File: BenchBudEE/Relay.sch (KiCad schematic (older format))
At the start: 0 parts

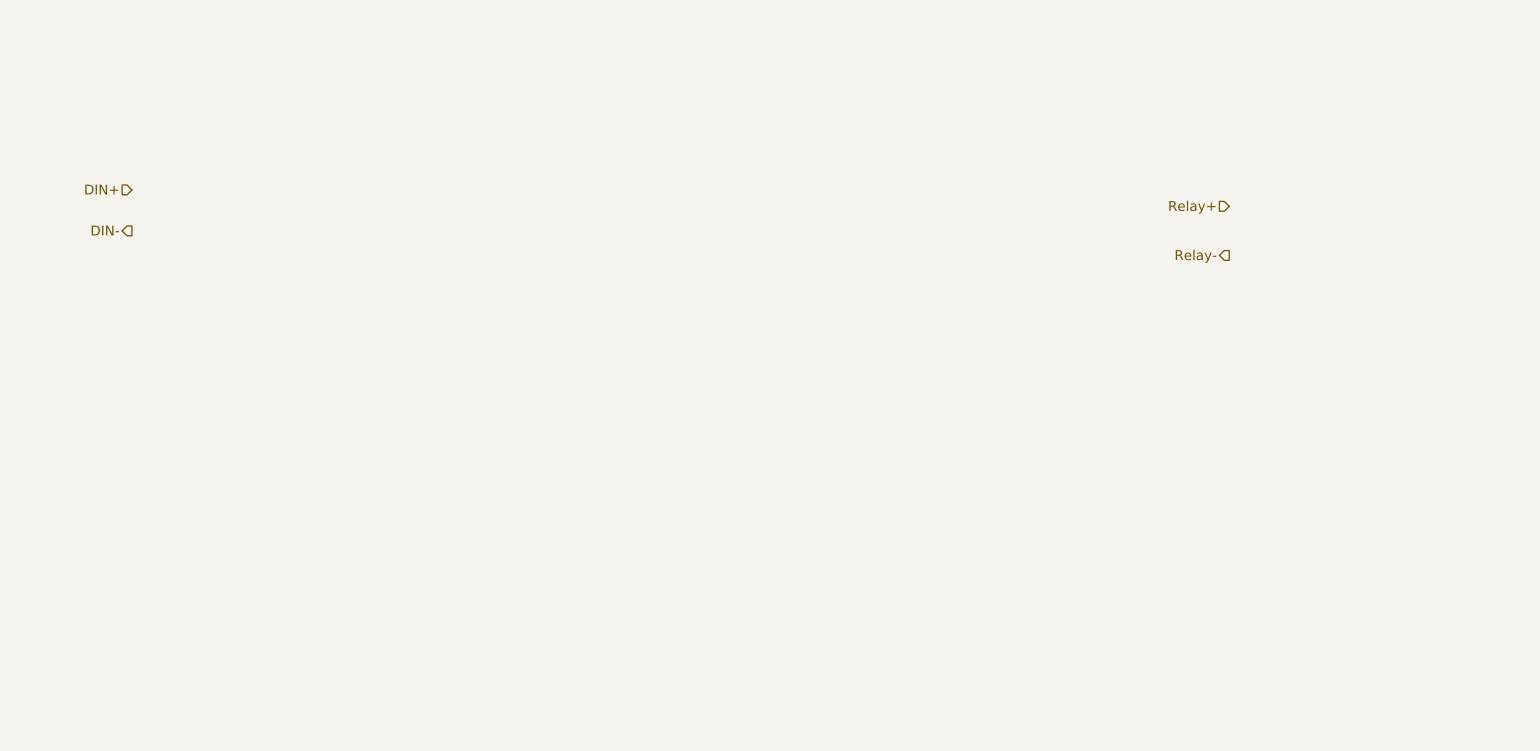
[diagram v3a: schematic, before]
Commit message: Roughly filled in the Relay sheet.
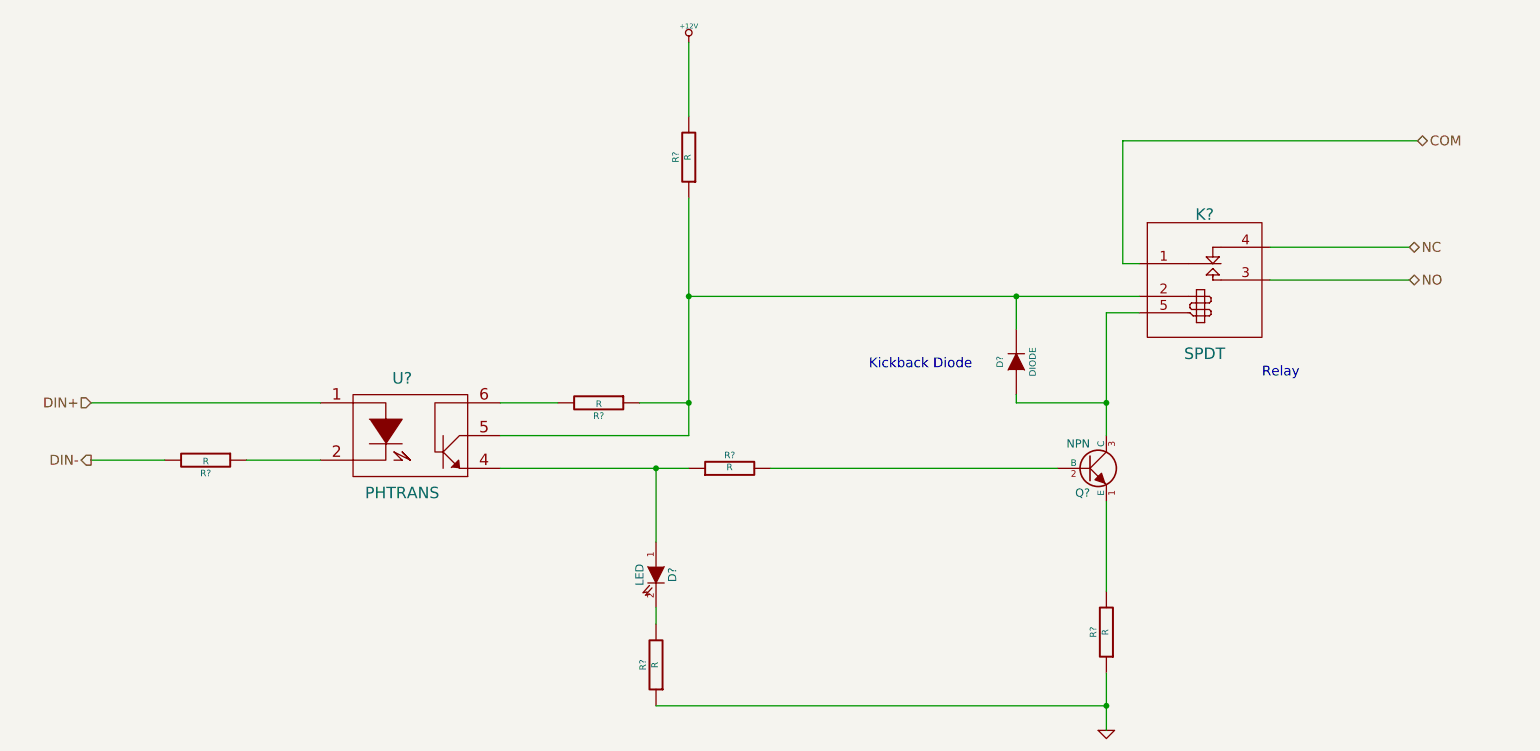
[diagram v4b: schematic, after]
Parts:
- added D?: LED, ~, symbol LED
- added D?: DIODE, ~, symbol DIODE
- added K?: SPDT, ~, symbol SPDT
- added Q?: NPN, ~, symbol NPN
- added R? (x6): R, ~, symbol R
- added U?: PHTRANS, ~, symbol PHTRANS
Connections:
- net DIN+: now also U?.1
- net DIN-: now also R?.2
- new net: R?.1, U?.2
- new net: D?.1 (A), R?.1, U?.4
- new net: D?.2 (K), K?.2 (COIL+), R?.1, R?.1, U?.5
- new net: R?.2, U?.6
- new net: Q?.2 (B), R?.2
- new net: Q?.1 (E), R?.2
- new net: D?.1 (A), K?.5 (COIL-), Q?.3 (C)
- new net: D?.2 (K), R?.2
- new net +12V: R?.2
- new net COM: K?.1 (COM)
- new net GND: R?.1, R?.1
- new net NC: K?.4 (NC)
- new net NO: K?.3 (NO)
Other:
- note added: "Kickback Diode"
- note added: "Relay"
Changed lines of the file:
@@
 LIBS:contrib
 LIBS:valves
+LIBS:BenchBudEE
 LIBS:BenchBudEE-cache
 EELAYER 27 0
@@
 Sheet 4 8
 Title ""
-Date "6 feb 2014"
+Date "7 feb 2014"
 Rev ""
 Comp ""
@@
 Comment4 ""
 $EndDescr
-Text HLabel 2100 2850 0    60   Input ~ 0
+Text HLabel 1850 4150 0    60   Input ~ 0
 DIN+
-Text HLabel 2100 3100 0    60   Output ~ 0
+Text HLabel 1850 4500 0    60   Output ~ 0
 DIN-
-Text HLabel 8800 2950 0    60   Input ~ 0
-Relay+
-Text HLabel 8800 3250 0    60   Output ~ 0
-Relay-
+Text HLabel 9900 3200 2    60   BiDi ~ 0
+NC
+Text HLabel 9900 3400 2    60   BiDi ~ 0
+NO
+$Comp
+L PHTRANS U?
+U 1 1 52F440BD
+P 3800 4350
+F 0 "U?" H 3750 4700 70  0000 C CNN
+F 1 "PHTRANS" H 3750 4000 70  0000 C CNN
+F 2 "~" H 3800 4350 60  0000 C CNN
+F 3 "~" H 3800 4350 60  0000 C CNN
+	1    3800 4350
+	1    0    0    -1
+$EndComp
+$Comp
+L R R?
+U 1 1 52F440DB
+P 5750 4550
+F 0 "R?" V 5830 4550 40  0000 C CNN
+F 1 "R" V 5757 4551 40  0000 C CNN
+F 2 "~" V 5680 4550 30  0000 C CNN
+F 3 "~" H 5750 4550 30  0000 C CNN
+	1    5750 4550
+	0    -1   -1   0
+$EndComp
+$Comp
+L NPN Q?
+U 1 1 52F440EA
+P 7950 4550
+F 0 "Q?" H 7950 4400 50  0000 R CNN
+F 1 "NPN" H 7950 4700 50  0000 R CNN
+F 2 "~" H 7950 4550 60  0000 C CNN
+F 3 "~" H 7950 4550 60  0000 C CNN
+	1    7950 4550
+	1    0    0    -1
+$EndComp
+$Comp
+L LED D?
+U 1 1 52F440F9
+P 5300 5200
+F 0 "D?" H 5300 5300 50  0000 C CNN
+F 1 "LED" H 5300 5100 50  0000 C CNN
+F 2 "~" H 5300 5200 60  0000 C CNN
+F 3 "~" H 5300 5200 60  0000 C CNN
+	1    5300 5200
+	0    1    1    0
+$EndComp
+$Comp
+L SPDT K?
+U 1 1 52F44639
+P 8650 3250
+F 0 "K?" H 8650 3500 70  0000 C CNN
+F 1 "SPDT" H 8650 2650 70  0000 C CNN
+F 2 "~" H 8650 3250 60  0000 C CNN
+F 3 "~" H 8650 3250 60  0000 C CNN
+	1    8650 3250
+	1    0    0    -1
+$EndComp
+Text HLabel 9950 2550 2    60   BiDi ~ 0
+COM
+Wire Wire Line
+	9050 3200 9900 3200
+Wire Wire Line
+	9050 3400 9900 3400
+Wire Wire Line
+	4350 4550 5500 4550
+Wire Wire Line
+	6000 4550 7750 4550
+Wire Wire Line
+	5500 3500 8250 3500
+Wire Wire Line
+	8050 4750 8050 5300
+$Comp
+L R R?
+U 1 1 52F448EE
+P 8050 5550
+F 0 "R?" V 8130 5550 40  0000 C CNN
+F 1 "R" V 8057 5551 40  0000 C CNN
+F 2 "~" V 7980 5550 30  0000 C CNN
+F 3 "~" H 8050 5550 30  0000 C CNN
+	1    8050 5550
+	-1   0    0    1
+$EndComp
+$Comp
+L GND #PWR?
+U 1 1 52F448F6
+P 8050 6150
+F 0 "#PWR?" H 8050 6150 30  0001 C CNN
+F 1 "GND" H 8050 6080 30  0001 C CNN
+F 2 "" H 8050 6150 60  0000 C CNN
+F 3 "" H 8050 6150 60  0000 C CNN
+	1    8050 6150
+	1    0    0    -1
+$EndComp
+Wire Wire Line
+	8050 5800 8050 6150
+Wire Wire Line
+	5500 2900 5500 4350
+Wire Wire Line
+	5300 5000 5300 4550
+Connection ~ 5300 4550
+$Comp
+L R R?
+U 1 1 52F44A66
+P 5300 5750
+F 0 "R?" V 5380 5750 40  0000 C CNN
+F 1 "R" V 5307 5751 40  0000 C CNN
+F 2 "~" V 5230 5750 30  0000 C CNN
+F 3 "~" H 5300 5750 30  0000 C CNN
+	1    5300 5750
+	-1   0    0    1
+$EndComp
+Wire Wire Line
+	5300 5500 5300 5400
+Wire Wire Line
+	5300 6000 8050 6000
+Connection ~ 8050 6000
+$Comp
+L R R?
+U 1 1 52F44A89
+P 5500 2650
+F 0 "R?" V 5580 2650 40  0000 C CNN
+F 1 "R" V 5507 2651 40  0000 C CNN
+F 2 "~" V 5430 2650 30  0000 C CNN
+F 3 "~" H 5500 2650 30  0000 C CNN
+	1    5500 2650
+	-1   0    0    1
+$EndComp
+$Comp
+L +12V #PWR?
+U 1 1 52F44A91
+P 5500 1950
+F 0 "#PWR?" H 5500 1900 20  0001 C CNN
+F 1 "+12V" H 5500 2050 30  0000 C CNN
+F 2 "" H 5500 1950 60  0000 C CNN
+F 3 "" H 5500 1950 60  0000 C CNN
+	1    5500 1950
+	1    0    0    -1
+$EndComp
+Wire Wire Line
+	5500 1950 5500 2400
+Wire Wire Line
+	5500 4350 4350 4350
+Connection ~ 5500 3500
+$Comp
+L R R?
+U 1 1 52F44ACB
+P 4950 4150
+F 0 "R?" V 5030 4150 40  0000 C CNN
+F 1 "R" V 4957 4151 40  0000 C CNN
+F 2 "~" V 4880 4150 30  0000 C CNN
+F 3 "~" H 4950 4150 30  0000 C CNN
+	1    4950 4150
+	0    1    1    0
+$EndComp
+Wire Wire Line
+	4350 4150 4700 4150
+Wire Wire Line
+	5200 4150 5500 4150
+Connection ~ 5500 4150
+$Comp
+L R R?
+U 1 1 52F44AFE
+P 2550 4500
+F 0 "R?" V 2630 4500 40  0000 C CNN
+F 1 "R" V 2557 4501 40  0000 C CNN
+F 2 "~" V 2480 4500 30  0000 C CNN
+F 3 "~" H 2550 4500 30  0000 C CNN
+	1    2550 4500
+	0    1    1    0
+$EndComp
+Wire Wire Line
+	2800 4500 3250 4500
+Wire Wire Line
+	1850 4500 2300 4500
+Wire Wire Line
+	1850 4150 3250 4150
+Wire Wire Line
+	9950 2550 8150 2550
+Wire Wire Line
+	8150 2550 8150 3300
+Wire Wire Line
+	8150 3300 8250 3300
+Wire Wire Line
+	8050 4350 8050 3600
+Wire Wire Line
+	8050 3600 8250 3600
+$Comp
+L DIODE D?
+U 1 1 52F44F61
+P 7500 3900
+F 0 "D?" H 7500 4000 40  0000 C CNN
+F 1 "DIODE" H 7500 3800 40  0000 C CNN
+F 2 "~" H 7500 3900 60  0000 C CNN
+F 3 "~" H 7500 3900 60  0000 C CNN
+	1    7500 3900
+	0    -1   -1   0
+$EndComp
+Wire Wire Line
+	7500 3700 7500 3500
+Connection ~ 7500 3500
+Wire Wire Line
+	7500 4100 7500 4150
+Wire Wire Line
+	7500 4150 8050 4150
+Connection ~ 8050 4150
+Text Notes 6600 3950 0    60   ~ 0
+Kickback Diode
+Text Notes 9000 4000 0    60   ~ 0
+Relay
 $EndSCHEMATC

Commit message: Roughly populated the Power sheet.
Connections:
- net +12V renamed +12P
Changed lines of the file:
@@
 $Descr A4 11693 8268
 encoding utf-8
-Sheet 4 8
+Sheet 4 9
 Title ""
-Date "7 feb 2014"
+Date "8 feb 2014"
 Rev ""
 Comp ""
@@
 	-1   0    0    1
 $EndComp
-$Comp
-L +12V #PWR?
-U 1 1 52F44A91
-P 5500 1950
-F 0 "#PWR?" H 5500 1900 20  0001 C CNN
-F 1 "+12V" H 5500 2050 30  0000 C CNN
-F 2 "" H 5500 1950 60  0000 C CNN
-F 3 "" H 5500 1950 60  0000 C CNN
-	1    5500 1950
-	1    0    0    -1
-$EndComp
-Wire Wire Line
-	5500 1950 5500 2400
+Wire Wire Line
+	5500 1900 5500 2400
 Wire Wire Line
 	5500 4350 4350 4350
@@
 Text Notes 9000 4000 0    60   ~ 0
 Relay
+$Comp
+L +12P #PWR?
+U 1 1 52F62CEB
+P 5500 1900
+F 0 "#PWR?" H 5500 1870 30  0001 C CNN
+F 1 "+12P" H 5500 2000 30  0000 C CNN
+F 2 "" H 5500 1900 60  0000 C CNN
+F 3 "" H 5500 1900 60  0000 C CNN
+	1    5500 1900
+	1    0    0    -1
+$EndComp
 $EndSCHEMATC

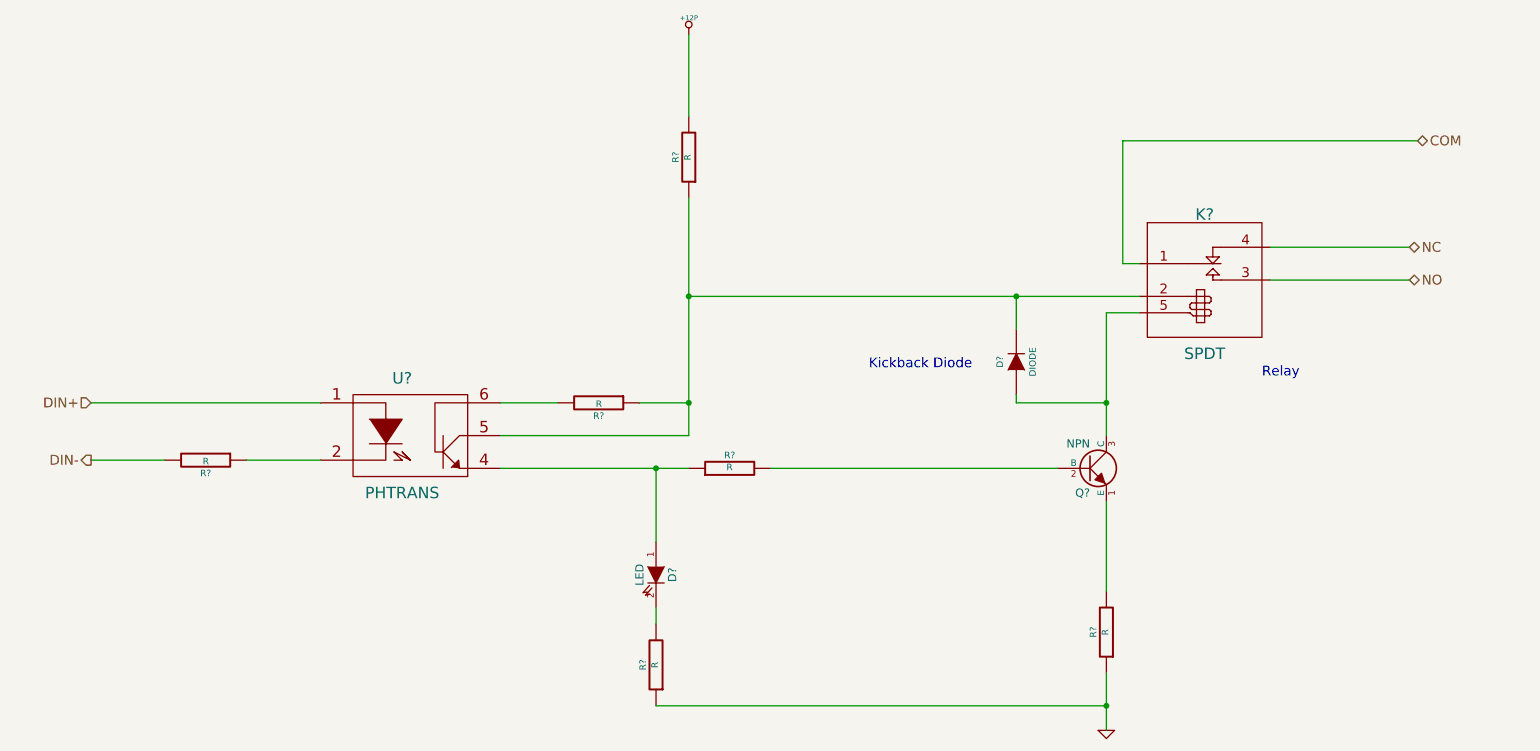
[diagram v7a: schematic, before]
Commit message: Populated the Arduino block and top level wiring.
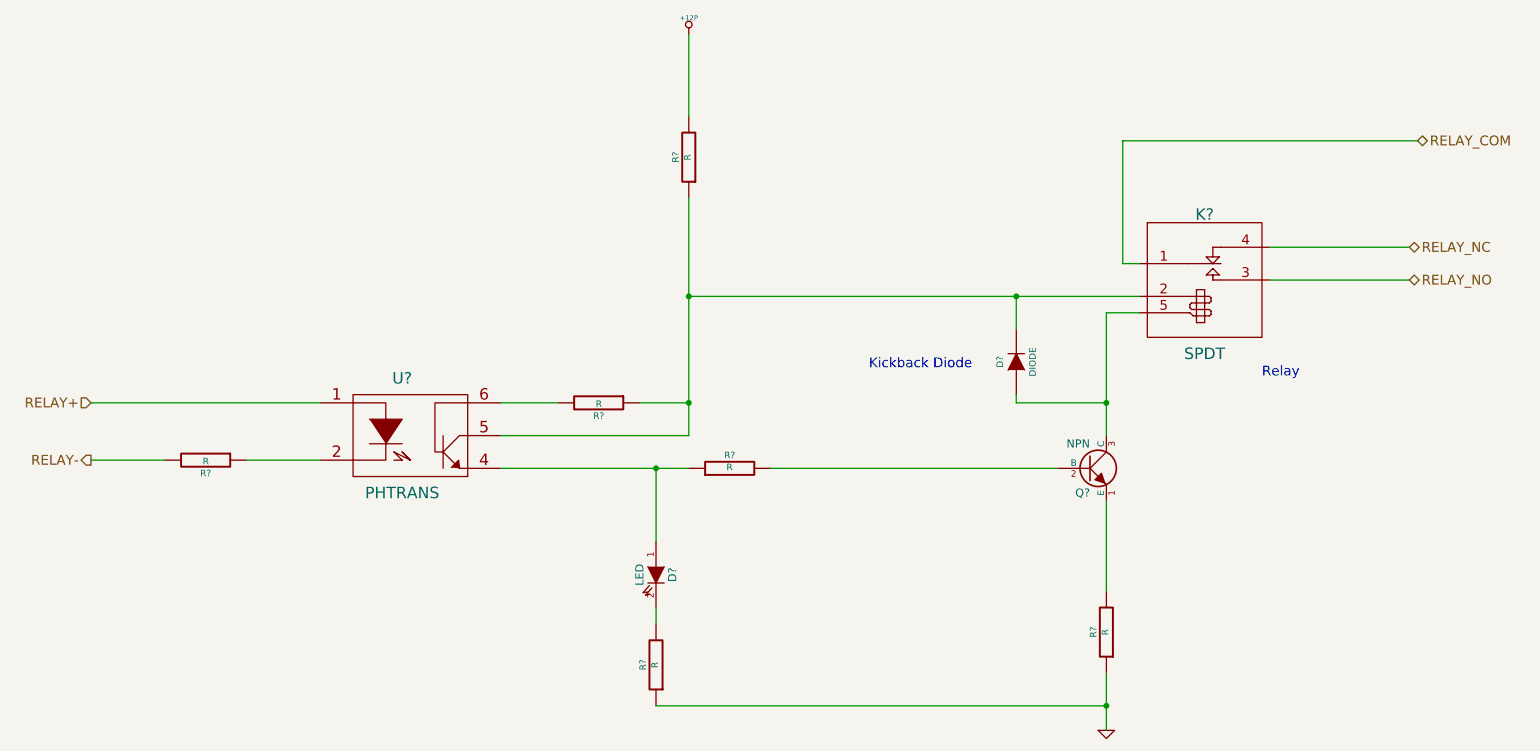
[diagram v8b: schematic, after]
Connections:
- net COM renamed RELAY_COM
- net DIN+ renamed RELAY+
- net DIN- renamed RELAY-
- net NC renamed RELAY_NC
- net NO renamed RELAY_NO
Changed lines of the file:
@@
 $EndDescr
 Text HLabel 1850 4150 0    60   Input ~ 0
-DIN+
+RELAY+
 Text HLabel 1850 4500 0    60   Output ~ 0
-DIN-
+RELAY-
 Text HLabel 9900 3200 2    60   BiDi ~ 0
-NC
+RELAY_NC
 Text HLabel 9900 3400 2    60   BiDi ~ 0
-NO
+RELAY_NO
 $Comp
 L PHTRANS U?
@@
 $EndComp
 Text HLabel 9950 2550 2    60   BiDi ~ 0
-COM
+RELAY_COM
 Wire Wire Line
 	9050 3200 9900 3200
